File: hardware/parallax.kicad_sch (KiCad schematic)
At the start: 14 parts, among them J1 Conn_Coaxial, J2 Conn_Coaxial, J3 Conn_Coaxial, J4 Conn_01x10_Pin, J5 Conn_01x02_Pin, SW2 SW_Push, U1 Pico

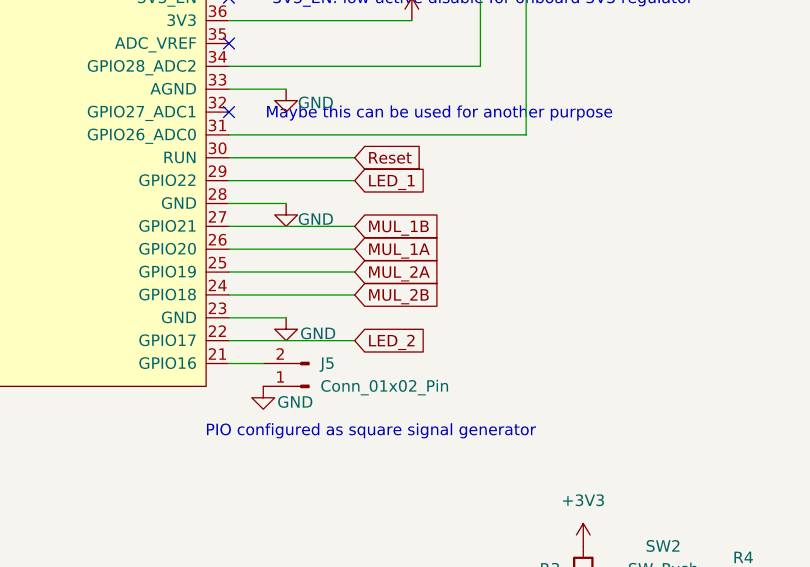
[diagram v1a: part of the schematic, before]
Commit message: reduced length of reference channel by 6mm
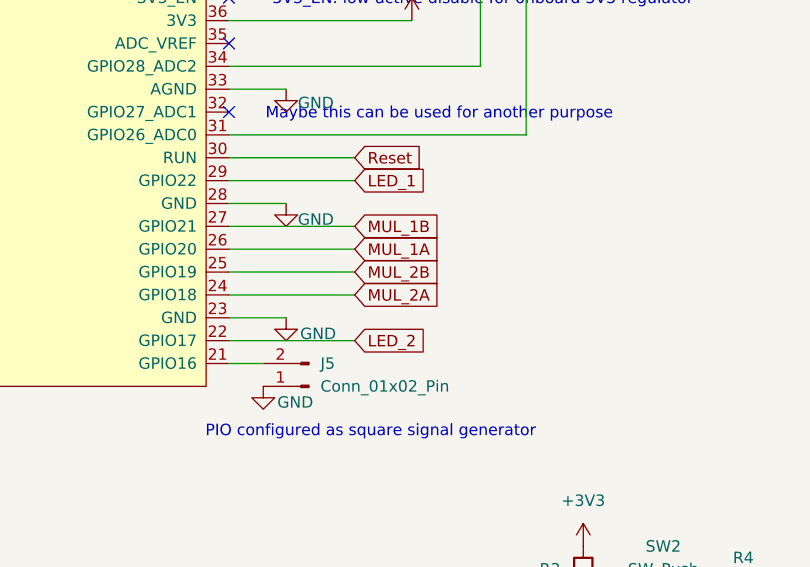
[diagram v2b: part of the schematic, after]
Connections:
- net MUL_2A: now also U1.24 (GPIO18); no longer U1.25 (GPIO19)
- net MUL_2B: now also U1.25 (GPIO19); no longer U1.24 (GPIO18)
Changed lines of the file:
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@@
 	(global_label "MUL_2A"
 		(shape input)
-		(at 226.06 105.41 0)
+		(at 226.06 107.95 0)
 		(fields_autoplaced yes)
 		(effects
@@
 		)
 		(property "Intersheetrefs" "${INTERSHEET_REFS}"
-			(at 236.1209 105.41 0)
+			(at 236.1209 107.95 0)
 			(hide yes)
 			(show_name no)
@@
 	(global_label "MUL_2B"
 		(shape input)
-		(at 226.06 107.95 0)
+		(at 226.06 105.41 0)
 		(fields_autoplaced yes)
 		(effects
@@
 		)
 		(property "Intersheetrefs" "${INTERSHEET_REFS}"
-			(at 236.3023 107.95 0)
+			(at 236.3023 105.41 0)
 			(hide yes)
 			(show_name no)
